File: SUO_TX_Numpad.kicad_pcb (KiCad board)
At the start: 2 copper layers, 79.1 x 127.6 mm, 93 parts, among them J1 USB_C_Receptacle_USB2.0_16P, SW1 BOOT, U1 STM32F411CEUx, U2 XC6206PxxxMR-Regulator_Linear, U3 USBLC6-2SC6

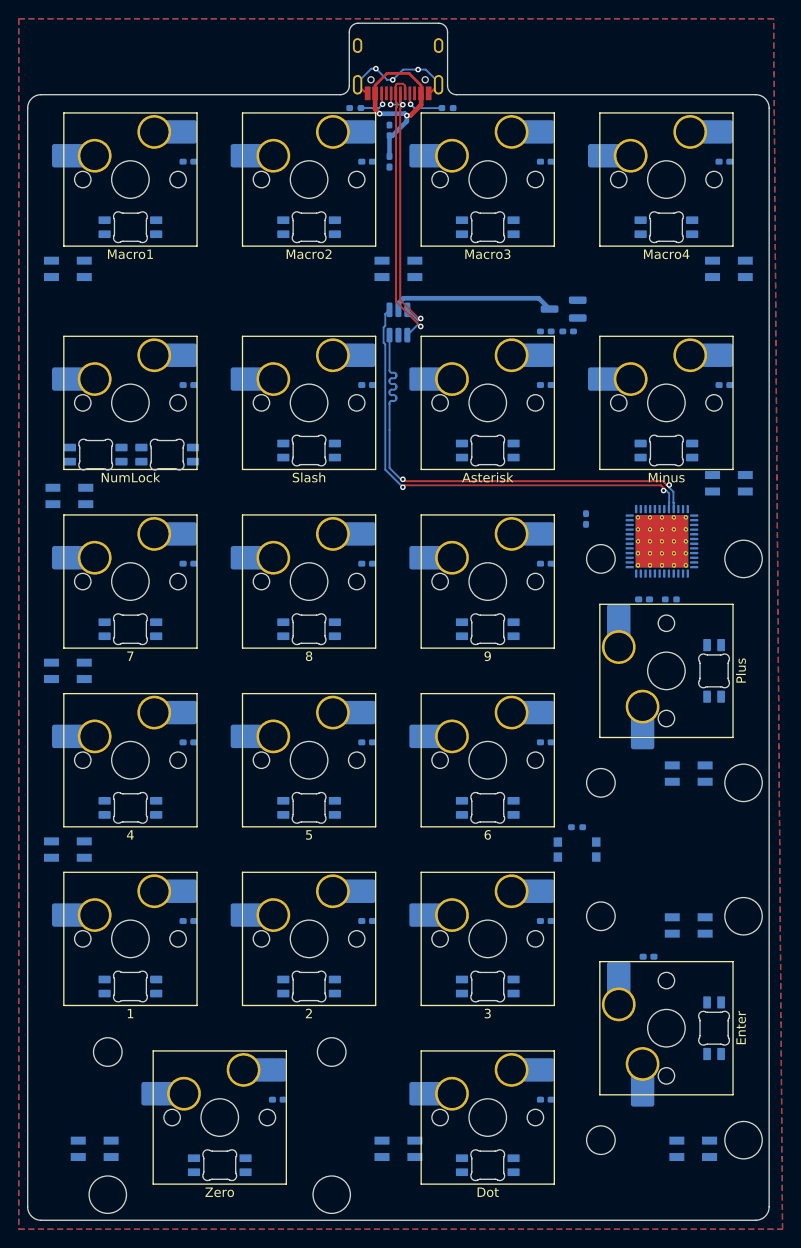
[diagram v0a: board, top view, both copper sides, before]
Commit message: Routing done, violations handled, Silk screen cleaned up
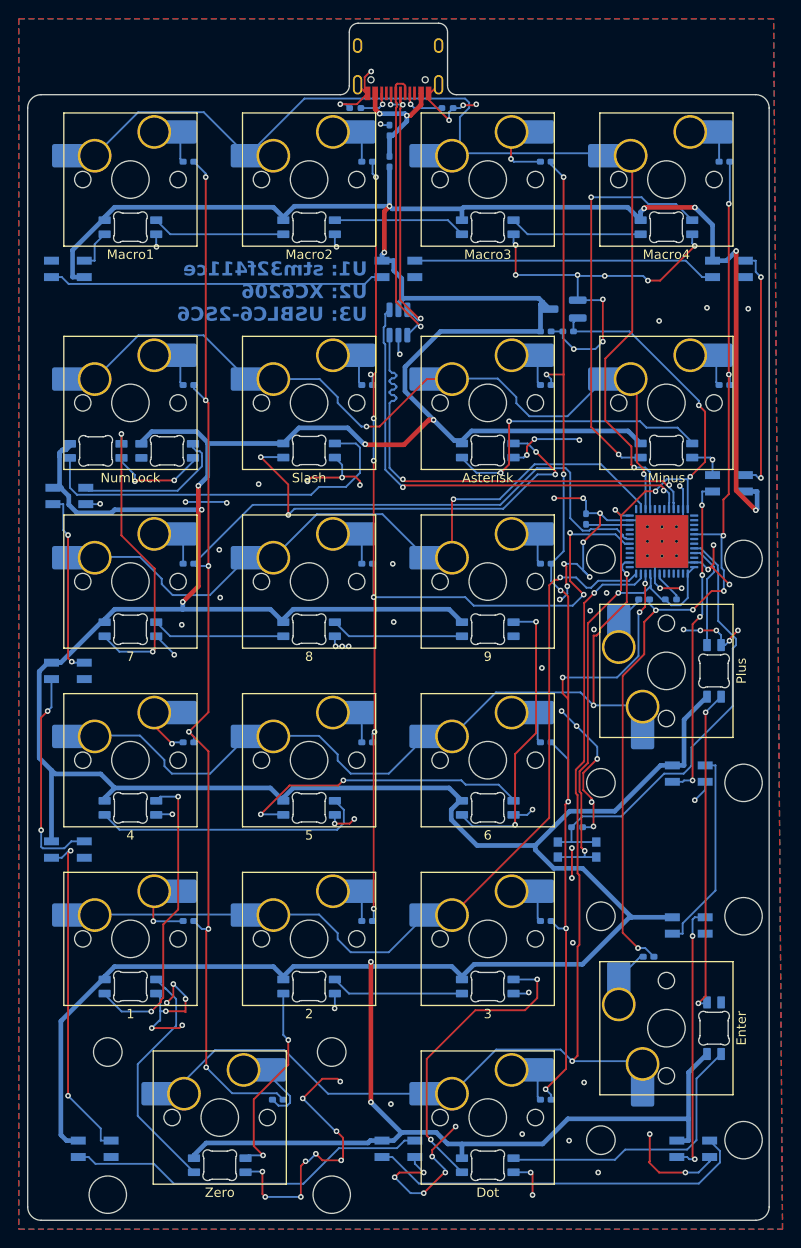
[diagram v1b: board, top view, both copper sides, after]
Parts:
- C1, C2, C3: value 10uF 16V -> 10uF
- C4: value 10pF 16V -> 10pF
- moved LED14 0.40 mm to (105.8, 66.7)
- moved LED22 0.40 mm to (113.5, 66.7)
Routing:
- net VBUS: track 17.5 -> 625.9 mm, vias 0 -> 13
- net GND: track 14.2 -> 289.0 mm, vias 3 -> 111
- net COL1: track 0.00 -> 172.6 mm, vias 0 -> 6
- net COL3: track 0.00 -> 136.1 mm, vias 0 -> 10
- net COL2: track 0.00 -> 125.0 mm, vias 0 -> 9
- net ROW1: track 0.00 -> 121.5 mm, vias 0 -> 1
- net ROW6: track 0.00 -> 119.0 mm, vias 0 -> 2
- net COL4: track 0.00 -> 100.4 mm, vias 0 -> 7
- net +3V3: track 0.00 -> 98.6 mm, vias 0 -> 6
- net ROW5: track 0.00 -> 94.8 mm, vias 0 -> 1
- net ROW4: track 0.00 -> 91.7 mm, vias 0 -> 2
- net ROW2: track 0.00 -> 89.4 mm, vias 0 -> 2
- net ROW3: track 0.00 -> 78.5 mm, vias 0 -> 1
- net Net-(U1-BOOT0): track 0.00 -> 48.6 mm
- net Net-(LED15-DOUT): track 0.00 -> 46.1 mm, vias 0 -> 4
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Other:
- board text added: "U1: stm32f411ce U2: XC6206 U3: USBLC6-2SC6"
